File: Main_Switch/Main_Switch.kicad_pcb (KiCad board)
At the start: 2 copper layers, 44.4 x 29.9 mm, 27 parts, among them J1 BAT+, J2 Load+, J3 Coil, J4 Switch, J5 Screw_Terminal_01x02, J6 Conn_ARM_SWD_TagConnect_TC2030, Q1 IRFR5410, Q2 2N7002, Q3 AO3400A, U1 CH32V003FxUx, U2 L78L05_SOT89, U4 LMR51610XDBVR

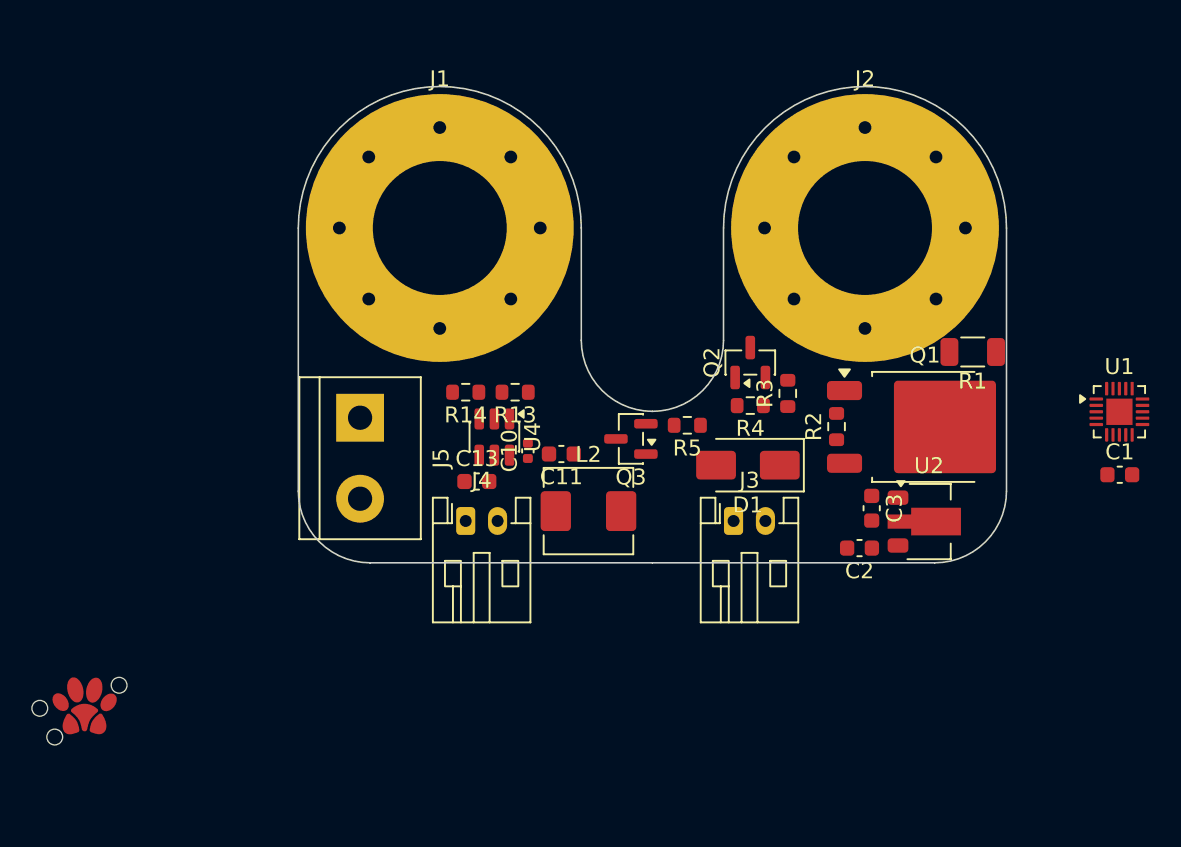
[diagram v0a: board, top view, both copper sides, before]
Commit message: enlarge PCB and fit LEDs + more caps
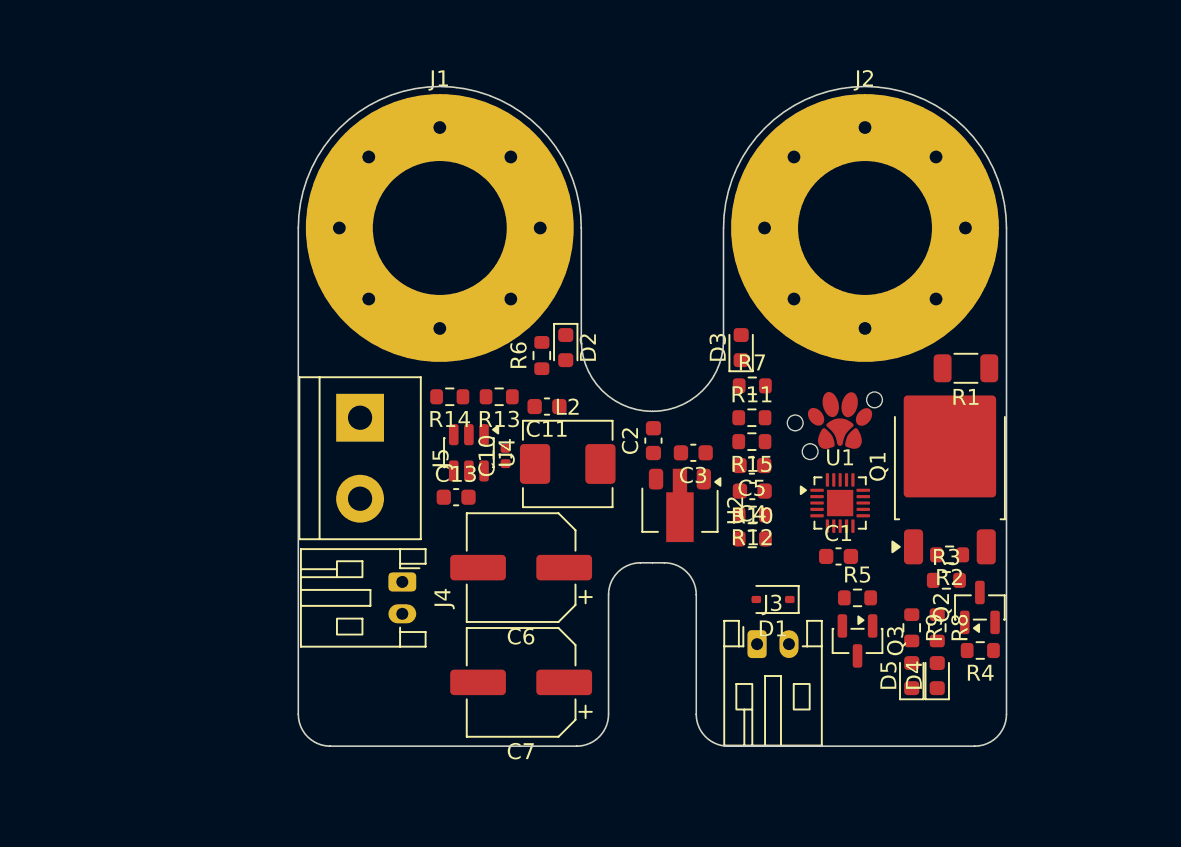
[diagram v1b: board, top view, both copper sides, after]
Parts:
- added C4: 100n, Capacitor_SMD:C_0603_1608Metric, F.Cu at (154.5, 110.9)
- added C5: 100n, Capacitor_SMD:C_0603_1608Metric, F.Cu at (154.4, 109.3)
- added C6: 220u 16V, Capacitor_SMD:CP_Elec_6.3x7.7, F.Cu at (140.0, 115.7)
- added C7: 220u 16V, Capacitor_SMD:CP_Elec_6.3x7.7, F.Cu at (140.0, 122.9)
- added D2: G_IN, LED_SMD:LED_0603_1608Metric, F.Cu at (142.8, 101.9)
- added D3: R_OUT, LED_SMD:LED_0603_1608Metric, F.Cu at (153.8, 101.9)
- added D4: B_PCHG, LED_SMD:LED_0603_1608Metric, F.Cu at (166.1, 122.4)
- added D5: W_LED, LED_SMD:LED_0603_1608Metric, F.Cu at (164.5, 122.4)
- added R10: 100k, Resistor_SMD:R_0603_1608Metric, F.Cu at (154.5, 113.9)
- added R11: 100k, Resistor_SMD:R_0603_1608Metric, F.Cu at (154.4, 106.3)
- added R12: 10k, Resistor_SMD:R_0603_1608Metric, F.Cu at (154.5, 112.4)
- added R15: 10k, Resistor_SMD:R_0603_1608Metric, F.Cu at (154.4, 107.8)
- added R6: 100k, Resistor_SMD:R_0603_1608Metric, F.Cu at (141.3, 102.4)
- added R7: 100k, Resistor_SMD:R_0603_1608Metric, F.Cu at (154.5, 104.3)
- added R8: 10k, Resistor_SMD:R_0603_1608Metric, F.Cu at (166.1, 119.4)
- added R9: 10k, Resistor_SMD:R_0603_1608Metric, F.Cu at (164.5, 119.4)
- D1: value SS34 -> B110WS; footprint Diode_SMD:D_SMA -> Diode_SMD:D_SOD-323
- J5: value Screw_Terminal_01x02 -> GND
- J6: value Conn_ARM_SWD_TagConnect_TC2030 -> PawConnect
- moved J6 50.6 mm to (159.7, 106.8)
- moved R4 21.1 mm to (168.8, 120.9)
- moved Q2 21.1 mm to (168.7, 118.2)
- moved Q3 19.0 mm to (161.1, 120.3), turned to -90 degrees
- moved U1 18.4 mm to (160.0, 111.6)
- moved C1 18.4 mm to (159.9, 115.0)
- moved U2 15.6 mm to (149.9, 112.1), turned to -90 degrees
- moved R3 15.4 mm to (166.6, 116.5), turned to 0 degrees
- moved R5 15.2 mm to (161.1, 117.6), turned to 0 degrees
- moved C2 14.6 mm to (148.3, 107.7), turned to 90 degrees
- moved C3 11.7 mm to (150.8, 108.5), turned to 180 degrees
- moved R2 10.7 mm to (166.8, 114.9), turned to 180 degrees
- moved D1 8.57 mm to (155.8, 117.7)
- moved J3 7.86 mm to (154.8, 120.5)
- moved J4 5.52 mm to (132.5, 116.6), turned to -90 degrees
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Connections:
- net /BUCK_VIN renamed BUCK_VIN
- net Net-(J2-Pad1) renamed OUT+
- Q2 pad 1: Net-(Q2-G) -> PRECHARGE
- Q3 pad 1: Net-(Q3-G) -> CONTACTOR
- R4 pad 2: Net-(Q2-G) -> PRECHARGE
- R5 pad 2: Net-(Q3-G) -> CONTACTOR
- U1 pad 10: unconnected-(U1-PC3-Pad10) -> CONTACTOR
- U1 pad 11: unconnected-(U1-PC4-Pad11) -> LED
- U1 pad 12: unconnected-(U1-PC5-Pad12) -> PRECHARGE
- U1 pad 2: unconnected-(U1-PA1-Pad2) -> SNS_VOUT
- U1 pad 3: unconnected-(U1-PA2-Pad3) -> SNS_VIN
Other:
- board size 44.4 x 29.9 mm -> 44.4 x 41.4 mm

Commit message: first revision done
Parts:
- added G***: LOGO, LeoDJ-kicad:Logo_PCBDerg_Mask_10mm, B.Cu at (139.3, 120.4)
- C6, C7: value 220u 16V -> 470u 16V
- J6: value PawConnect -> TC2030
- moved C1 1.76 mm to (158.2, 114.6), turned to 180 degrees
- moved C3 1.55 mm to (151.0, 106.9)
- moved U2 1.54 mm to (150.0, 110.5)
- moved R6 1.28 mm to (140.5, 103.4), turned to 0 degrees
- moved C10 1.00 mm to (139.0, 107.7)
- moved C2 0.83 mm to (148.0, 106.9), turned to 180 degrees
- moved R7 0.10 mm to (154.6, 104.3)
- turned D1 to 0 degrees
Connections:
- J3 pad 1: Net-(D1-A) -> +12V
- J3 pad 2: +12V -> Net-(D1-A)
- J6 pad 6: unconnected-(J6-SWO-Pad6) -> TX
- J6 pad 7: (no net) -> RX
- U1 pad 19: unconnected-(U1-PD5-Pad19) -> TX
- U1 pad 20: unconnected-(U1-PD6-Pad20) -> RX
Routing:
- net BUCK_VIN: track 0.00 -> 50.5 mm, vias 0 -> 1
- net GND: track 0.00 -> 34.1 mm, vias 0 -> 31
- net +5V: track 0.00 -> 30.5 mm, vias 0 -> 2
- net BAT+: track 0.00 -> 29.2 mm, vias 0 -> 4
- net OUT+: track 0.00 -> 27.2 mm
- net +12V: track 0.00 -> 25.2 mm
- net PRECHARGE: track 0.00 -> 12.9 mm
- net NRST: track 0.00 -> 10.9 mm
- net LED: track 0.00 -> 7.92 mm
- net Net-(D1-A): track 0.00 -> 7.43 mm
- net SNS_VOUT: track 0.00 -> 7.14 mm
- net CONTACTOR: track 0.00 -> 6.78 mm
- net SNS_VIN: track 0.00 -> 6.62 mm
- net Net-(Q1-D): track 0.00 -> 5.92 mm
- net SWDIO: track 0.00 -> 5.65 mm
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- added copper zone on F.Cu, net +12V
- added copper zone on B.Cu, net BAT+
- added copper zone on F.Cu, net BUCK_VIN
- added copper zone on B.Cu, net GND
- added copper zone on F.Cu, net GND
- added copper zone on In1.Cu, net GND
- added copper zone on In2.Cu, net GND
- added copper zone on F.Cu, net Net-(U4-SW)
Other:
- copper layers 2 -> 4
- board text added: "+"
- board text added: "Coil"
- board text added: "GND"
- board text added: "IN"
- board text added: "OUT"
- board text added: "PRECHG"
- board text added: "Pre-Charge PCB v1.0 ~by LeoDJ"
- board text added: "STATUS"
- board text added: "Switch"
- board text added: "https://github.com/ RainbowLabsDE/Torquee"

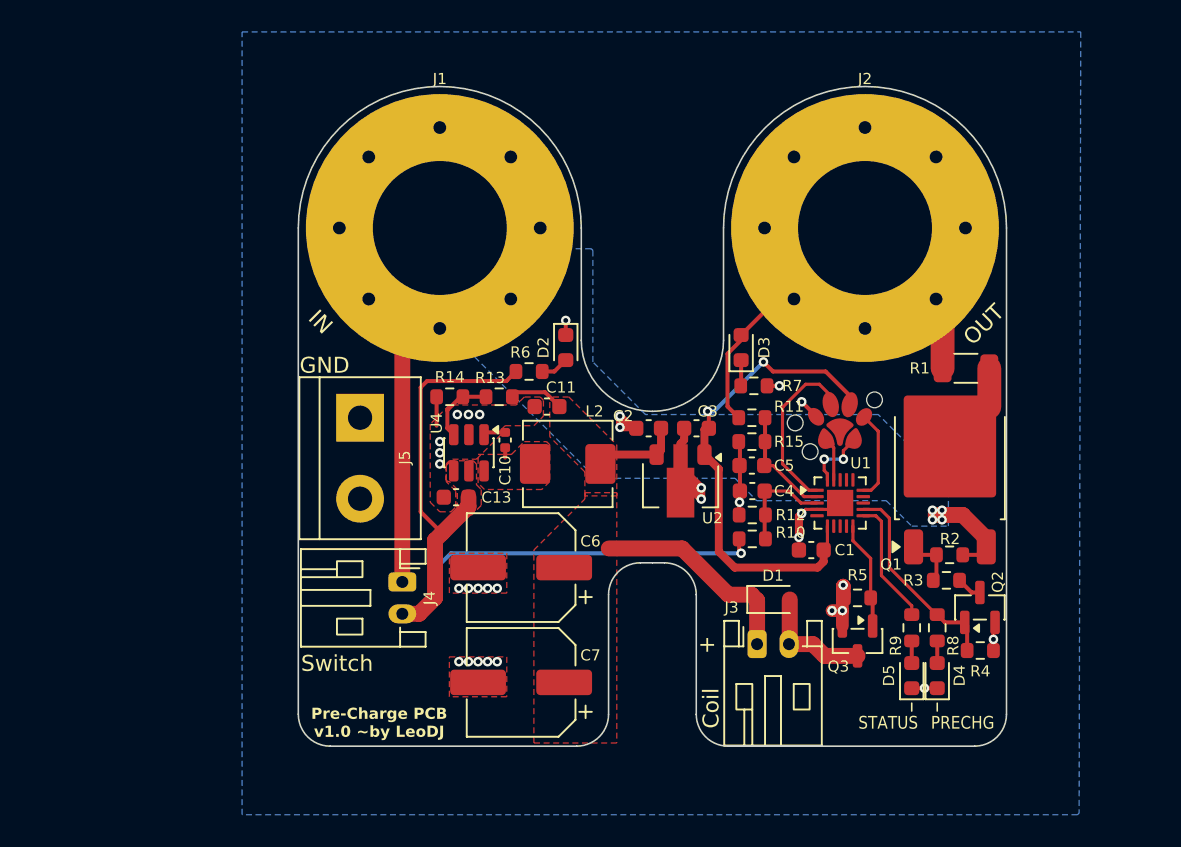
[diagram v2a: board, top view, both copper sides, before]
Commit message: switch to linear MOSFET pre-charge approach
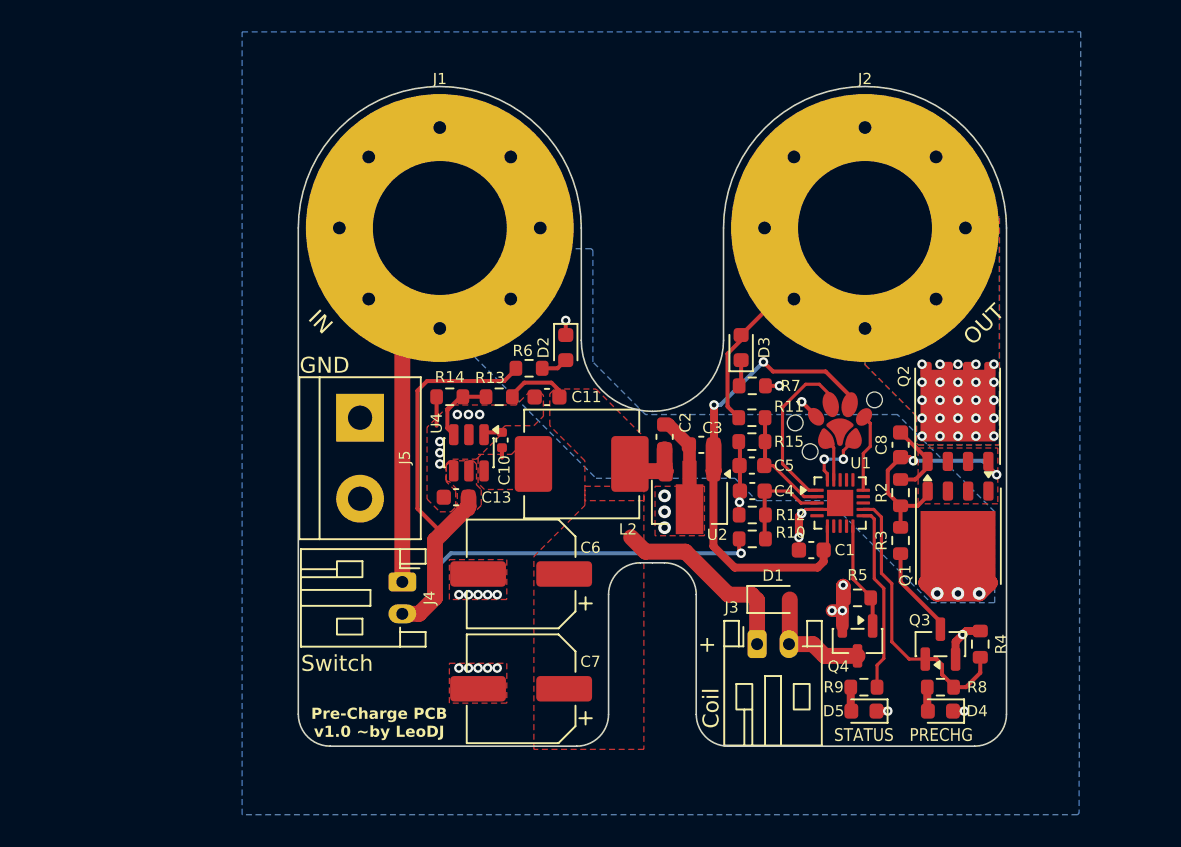
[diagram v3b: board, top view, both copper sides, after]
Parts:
- removed R1: 10, Resistor_SMD:R_1206_3216Metric
- added C8: 10u 25V, Capacitor_SMD:C_0603_1608Metric, F.Cu at (163.8, 108.0)
- added Q1: XR20P10F, Package_SON:Infineon_PG-TDSON-8_6.15x5.15mm, F.Cu at (167.4, 113.7)
- L2: value 22uH <250mOhm -> 68uH; footprint Inductor_SMD:L_Sunlord_MWSA0503S -> Inductor_SMD:L_Sunlord_MWSA0605S
- Q2: renamed from Q1; value IRFR5410 -> XR20P10F; footprint Package_TO_SOT_SMD:TO-252-2 -> Package_SON:Infineon_PG-TDSON-8_6.15x5.15mm
- R2: value 22k -> 120k
- R3: value 100k -> 1M
- moved R2 4.97 mm to (163.8, 111.0), turned to -90 degrees
- moved R9 4.78 mm to (161.5, 123.2), turned to 180 degrees
- moved R3 3.81 mm to (163.8, 114.0), turned to -90 degrees
- moved D5 3.74 mm to (161.5, 124.7), turned to 180 degrees
- moved R8 3.73 mm to (166.3, 123.2), turned to 180 degrees
- moved Q3 3.38 mm to (166.3, 120.5)
- moved Q2 3.18 mm to (167.4, 106.2)
- moved D4 2.23 mm to (166.3, 124.7), turned to 180 degrees
- moved U2 1.18 mm to (150.5, 111.6)
- moved C2 1.14 mm to (149.0, 107.5), turned to 90 degrees
- moved C3 1.08 mm to (151.3, 108.0)
- moved L2 0.88 mm to (143.8, 109.2)
- moved C11 0.60 mm to (141.6, 105.0)
- moved C7 0.40 mm to (140.0, 123.3)
- moved C6 0.40 mm to (140.0, 116.1)
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- renumbered Q2 to Q3, Q3 to Q4
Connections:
- Q2 pad 1: Net-(Q1-G) -> Net-(C8-Pad1)
- Q2 pad 2: Net-(Q1-D) -> Net-(C8-Pad1)
- Q2 pad 3: BAT+ -> Net-(C8-Pad1)
- R2 pad 1: BAT+ -> Net-(C8-Pad1)
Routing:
- net Net-(Q1-G): track 3.32 -> 14.9 mm, vias 0 -> 2
- net OUT+: track 27.2 -> 16.4 mm, vias 0 -> 25
- net Net-(Q1-D): track 5.92 -> 0.00 mm
- net GND: track 34.1 -> 28.9 mm
- net PRECHARGE: track 12.9 -> 17.9 mm
- net Net-(C8-Pad1): track 0.00 -> 4.91 mm
- net Net-(Q3-D): track 1.59 -> 5.77 mm
- net LED: track 7.92 -> 11.7 mm
- net BAT+: track 29.2 -> 31.7 mm, vias 4 -> 3
- net +12V: track 25.2 -> 22.9 mm
- net SWDIO: track 5.65 -> 4.95 mm
- added copper zone on F.Cu, net Net-(C8-Pad1)
- added copper zone on B.Cu, net OUT+
- added copper zone on F.Cu, net OUT+
- added copper zone on In1.Cu, net OUT+
- added copper zone on In2.Cu, net OUT+

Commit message: move FETs up (shorten power path)
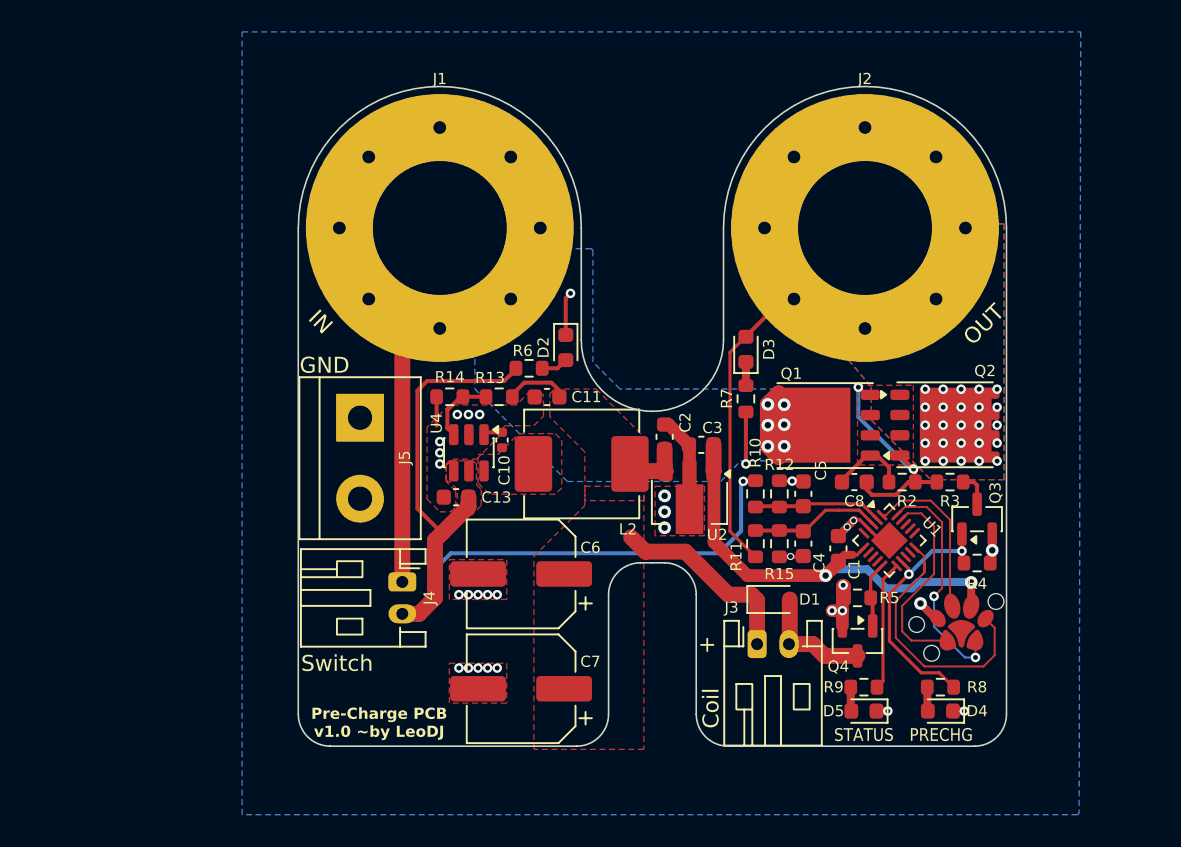
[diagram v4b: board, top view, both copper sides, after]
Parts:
- C11: value 22u 10V -> 22u 16V
- moved J6 14.8 mm to (167.3, 119.4)
- moved Q1 10.9 mm to (159.0, 106.7), turned to 180 degrees
- moved Q3 8.17 mm to (168.6, 112.6)
- moved R11 7.90 mm to (154.7, 114.2), turned to 90 degrees
- moved R15 6.63 mm to (156.2, 114.2), turned to -90 degrees
- moved C5 5.87 mm to (157.7, 114.2), turned to -90 degrees
- moved R4 5.09 mm to (168.6, 115.4), turned to 180 degrees
- moved R3 4.80 mm to (166.9, 110.3), turned to 0 degrees
- moved U1 3.88 mm to (163.1, 114.0), turned to -45 degrees
- moved C8 3.72 mm to (160.9, 110.3), turned to 0 degrees
- moved C4 3.20 mm to (157.7, 111.0), turned to 90 degrees
- moved R10 2.83 mm to (154.7, 111.0), turned to -90 degrees
- moved R12 2.16 mm to (156.2, 111.0), turned to 90 degrees
- moved C1 1.70 mm to (159.9, 114.5), turned to 90 degrees
- moved Q2 0.98 mm to (166.6, 106.7), turned to 0 degrees
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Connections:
- U1 pad 2: SNS_VOUT -> SNS_VIN
- U1 pad 3: SNS_VIN -> SNS_VOUT
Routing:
- net SWDIO: track 4.95 -> 17.7 mm
- net RX: track 4.06 -> 14.6 mm
- net TX: track 2.70 -> 13.1 mm
- net OUT+: track 16.4 -> 25.2 mm
- net LED: track 11.7 -> 8.12 mm
- net Net-(Q3-D): track 5.77 -> 2.15 mm
- net BUCK_VIN: track 50.8 -> 54.4 mm
- net CONTACTOR: track 6.78 -> 4.12 mm
- net SNS_VIN: track 6.62 -> 8.15 mm
- net +5V: track 30.1 -> 28.7 mm
- net PRECHARGE: track 17.9 -> 16.7 mm, vias 0 -> 2
- net SNS_VOUT: track 7.14 -> 8.31 mm
- net GND: track 28.9 -> 29.7 mm, vias 31 -> 32
- net Net-(U4-SW): track 0.62 -> 0.00 mm
- net BAT+: vias 3 -> 6
